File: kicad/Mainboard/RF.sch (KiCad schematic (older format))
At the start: 100 parts, among them J8 Antenna, Q3 BGA6589, T1 AFT05MS004NT1, U5 ADF7021, U6 HMC546MS8GETR, U7 LM2904A, X1 12.288MHz

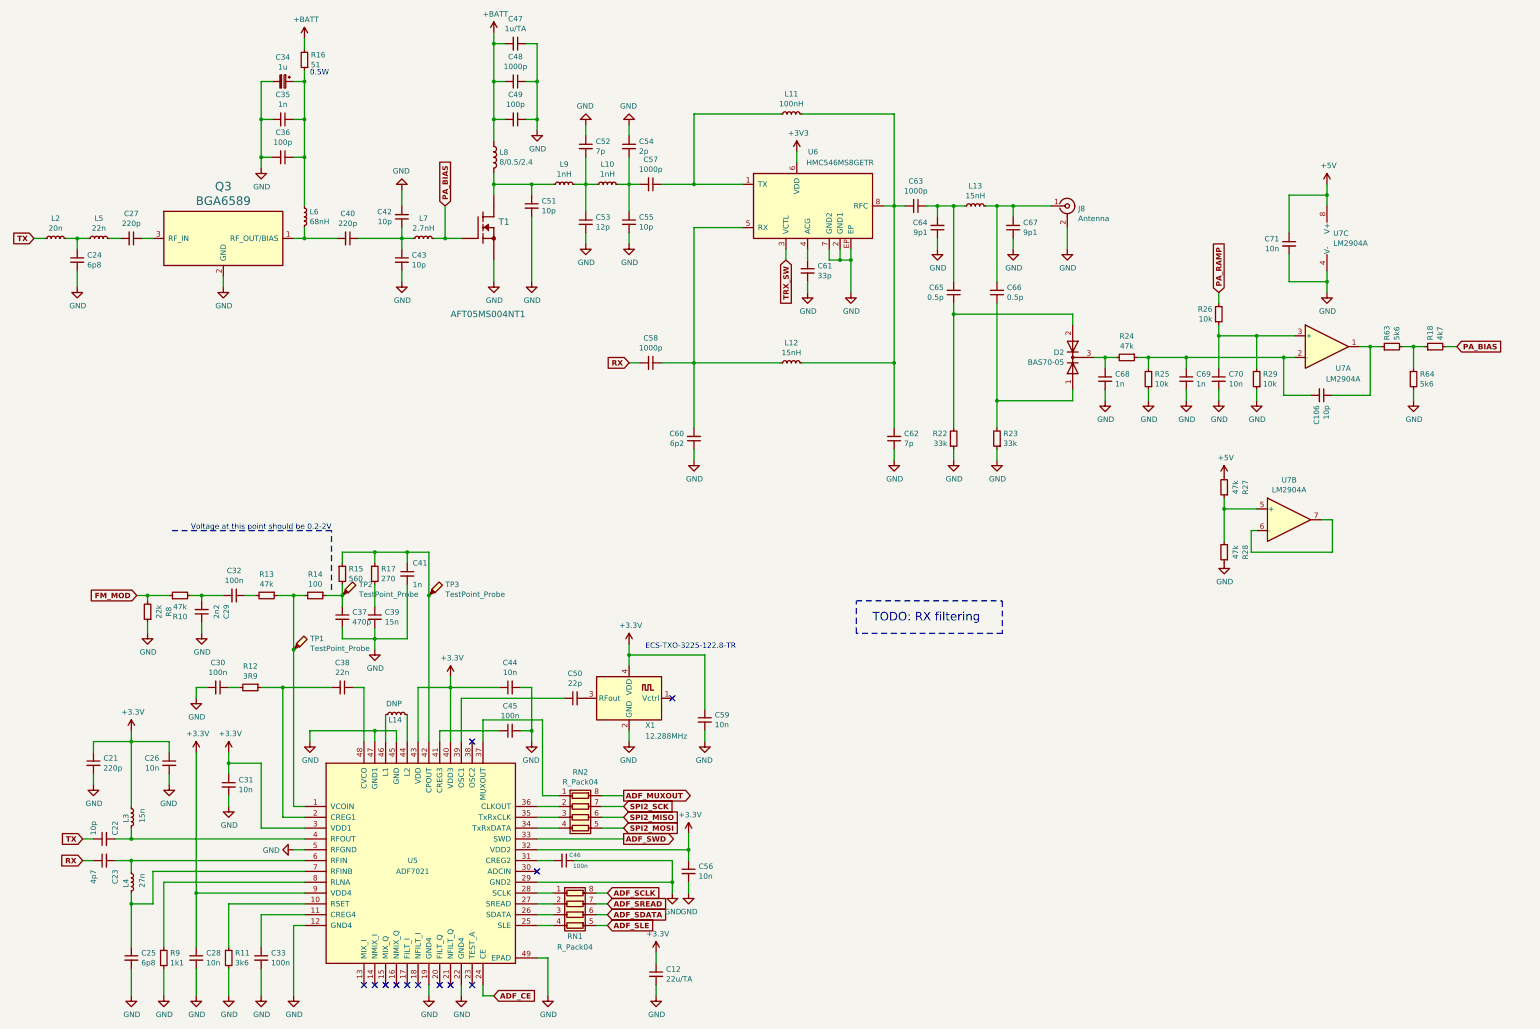
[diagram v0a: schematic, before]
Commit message: added 6 testpoints
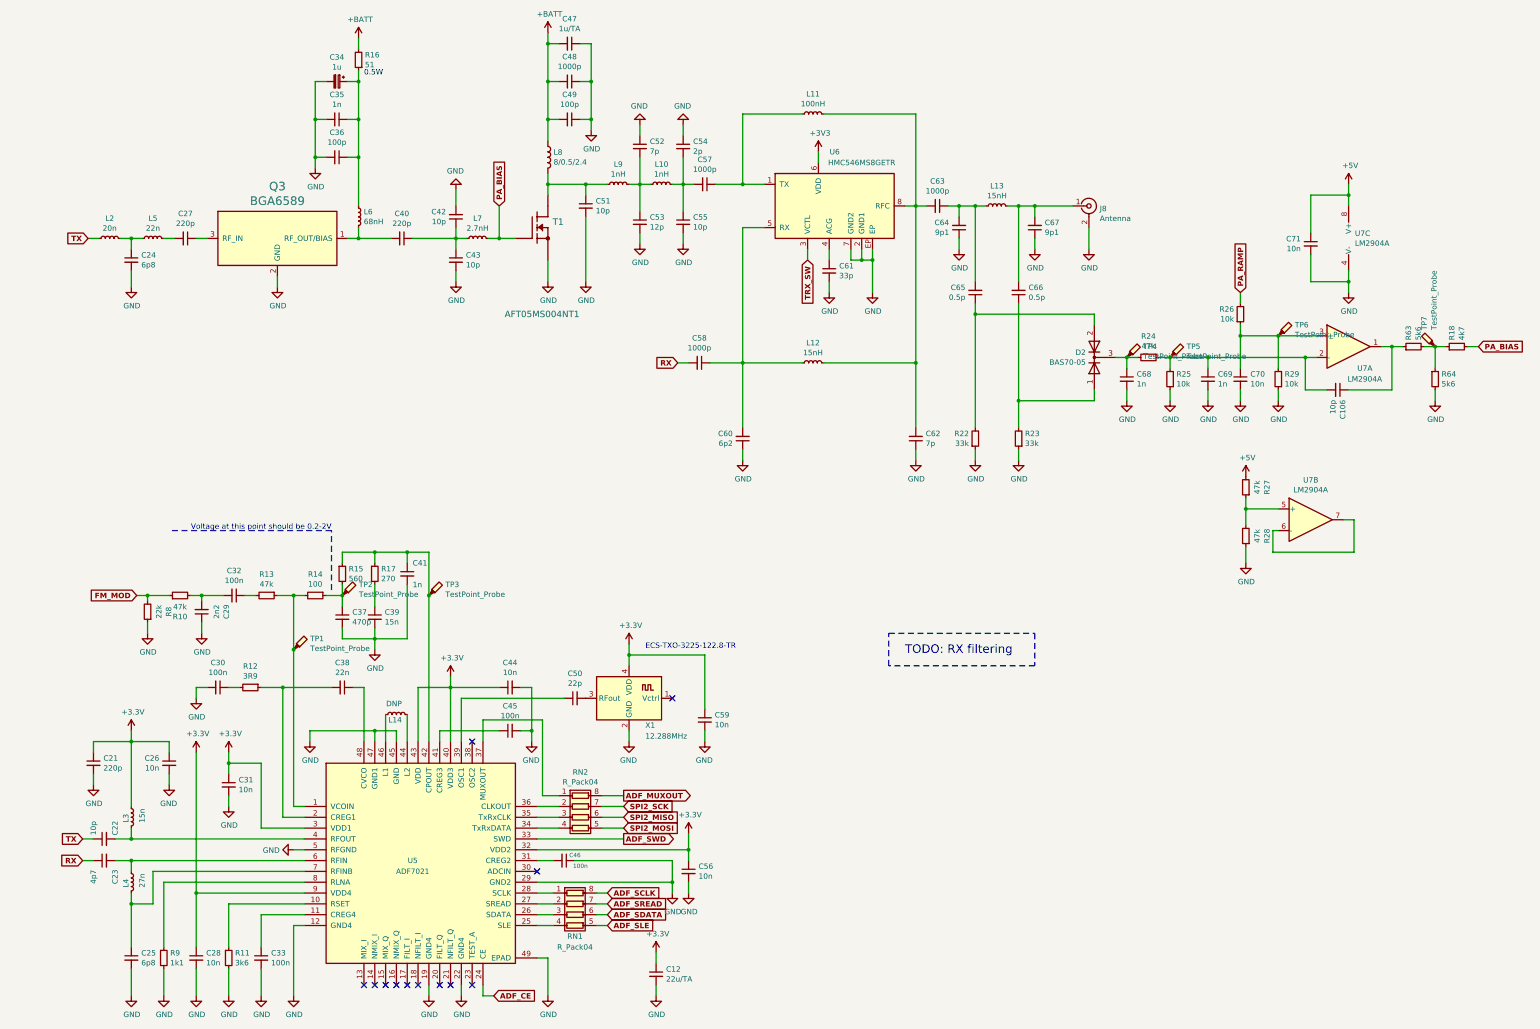
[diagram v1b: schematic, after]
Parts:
- removed C106: 10p, Capacitor_SMD:C_0603_1608Metric, symbol Mainboard-rescue:C_Small-device
- added C106: 10p, Capacitor_SMD:C_0603_1608Metric, symbol Mainboard-rescue:C_Small-Device
- added TP4, TP5, TP6, TP7: TestPoint_Probe, TestPoint:TestPoint_Pad_D1.0mm, symbol Mainboard-rescue:TestPoint_Probe-Connector
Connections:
- net at R18.1, R63.2, R64.1: now also TP7.1
- net at C68.1, D2.3 (K), R24.2: now also TP4.1
- net at C69.1, R24.1, R25.2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: now also C106.2, TP5.1
- net at R63.1, U7.1: now also C106.1
- net at C70.1, R26.1, R29.2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: now also TP6.1
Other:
- moved on the sheet: C24, C27, C34, C35, C36, C40, C42, C43, C47, C48, C49, C51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

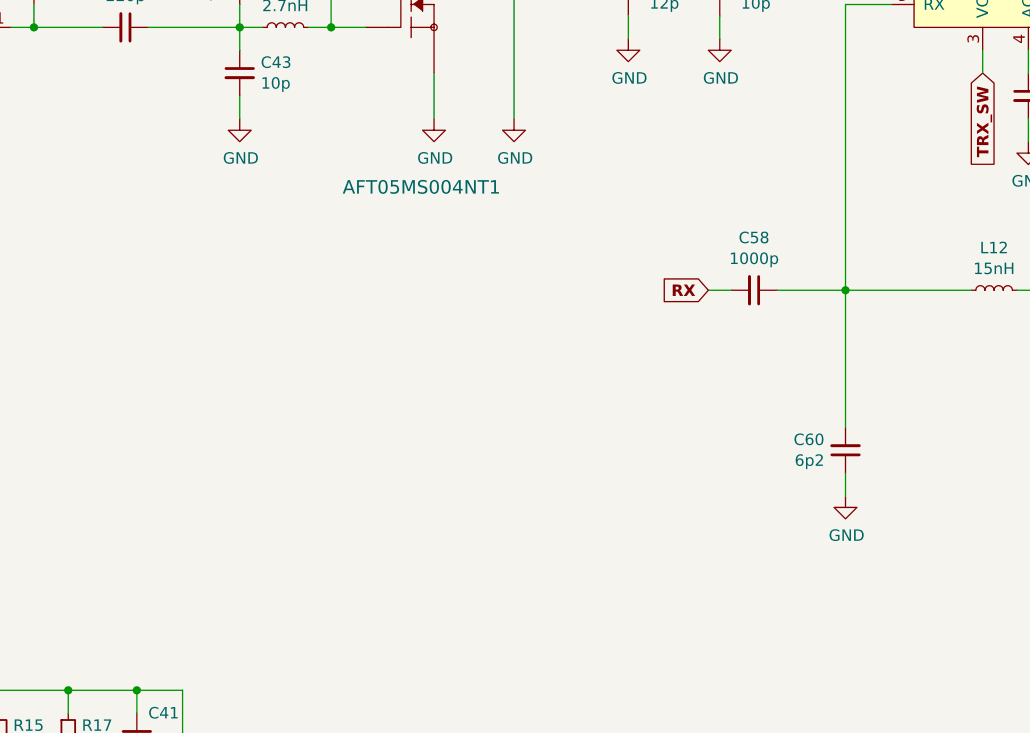
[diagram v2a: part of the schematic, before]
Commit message: added BGA2874 RX amplifier & highpass LC filter(schematic & pcb) pcb design nearly done ~95%
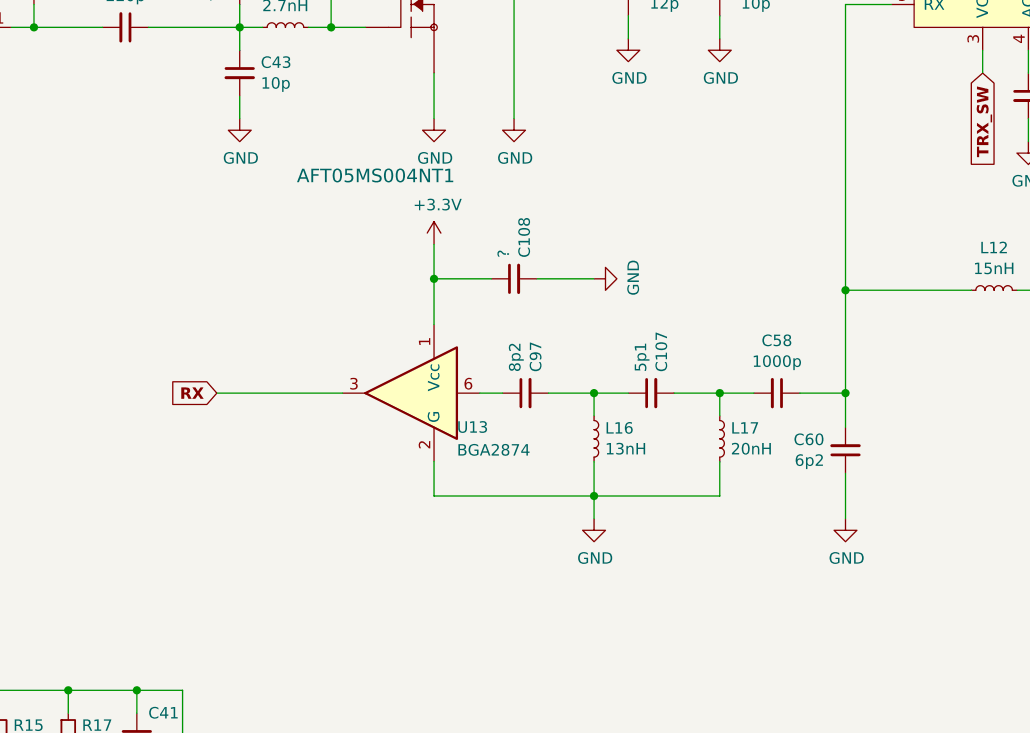
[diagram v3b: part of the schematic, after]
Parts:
- added C107: 5p1, Capacitor_SMD:C_0603_1608Metric, symbol Mainboard-rescue:C_Small-Device
- added C108: ?, Capacitor_SMD:C_0603_1608Metric, symbol Mainboard-rescue:C_Small-Device
- added C97: 8p2, Capacitor_SMD:C_0603_1608Metric, symbol Mainboard-rescue:C_Small-Device
- added L16: 13nH, Inductor_SMD:L_0603_1608Metric, symbol Device:L_Small
- added L17: 20nH, Inductor_SMD:L_0603_1608Metric, symbol Device:L_Small
- added U13: BGA2874, Package_TO_SOT_SMD:SOT-363_SC-70-6, symbol RF_Amplifier:BGA2874
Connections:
- net +3V3: now also C108.1, U13.1 (Vcc)
- net GND: now also C108.2, L16.2, L17.2, U13.2 (G), U13.4 (G), U13.5 (G)
- net RX: now also U13.3; no longer C58.2
- new net: C107.2, C58.2, L17.1
- new net: C97.1, U13.6
- new net: C107.1, C97.2, L16.1
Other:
- moved on the sheet: C58
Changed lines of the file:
@@
 EESchema Schematic File Version 4
-LIBS:Mainboard-cache
 EELAYER 30 0
 EELAYER END
@@
 P 6250 2900
 F 0 "T1" H 6394 2953 59  0000 L CNN
-F 1 "AFT05MS004NT1" H 5950 2100 59  0000 L CNN
+F 1 "AFT05MS004NT1" H 5750 2150 59  0000 L CNN
 F 2 "TR-9:AFT05MS004NT1" H 6250 2900 50  0001 C CNN
 F 3 "" H 6250 2900 50  0001 C CNN
@@
 L Mainboard-rescue:C_Small-device C58
 U 1 1 5DF79664
-P 7750 4150
-F 0 "C58" V 7521 4150 50  0000 C CNN
-F 1 "1000p" V 7612 4150 50  0000 C CNN
-F 2 "Capacitor_SMD:C_0603_1608Metric" H 7750 4150 50  0001 C CNN
-F 3 "~" H 7750 4150 50  0001 C CNN
-	1    7750 4150
+P 7850 4600
+F 0 "C58" V 7621 4600 50  0000 C CNN
+F 1 "1000p" V 7712 4600 50  0000 C CNN
+F 2 "Capacitor_SMD:C_0603_1608Metric" H 7850 4600 50  0001 C CNN
+F 3 "~" H 7850 4600 50  0001 C CNN
+	1    7850 4600
 	0    1    1    0
 $EndComp
@@
 Wire Wire Line
 	8150 2900 8150 4150
-Wire Wire Line
-	7650 4150 7550 4150
-Text GLabel 7550 4150 0    50   Input ~ 10
+Text GLabel 5400 4600 0    50   Input ~ 10
 RX
 Text GLabel 14950 4000 2    50   Input ~ 10
@@
 L power:GND #PWR098
 U 1 1 5E0A2231
-P 8150 5050
-F 0 "#PWR098" H 8150 4800 50  0001 C CNN
-F 1 "GND" H 8155 4877 50  0000 C CNN
-F 2 "" H 8150 5050 50  0001 C CNN
-F 3 "" H 8150 5050 50  0001 C CNN
-	1    8150 5050
-	1    0    0    -1
-$EndComp
-Wire Wire Line
-	8150 4950 8150 5050
-Wire Wire Line
-	8150 4150 8150 4750
+P 8150 5150
+F 0 "#PWR098" H 8150 4900 50  0001 C CNN
+F 1 "GND" H 8155 4977 50  0000 C CNN
+F 2 "" H 8150 5150 50  0001 C CNN
+F 3 "" H 8150 5150 50  0001 C CNN
+	1    8150 5150
+	1    0    0    -1
+$EndComp
+Wire Wire Line
+	8150 4150 8150 4600
 $Comp
 L Mainboard-rescue:C_Small-Device C62
@@
 	8150 2500 8350 2500
 Wire Wire Line
-	7850 4150 8150 4150
-Wire Wire Line
 	8150 4150 8700 4150
 Wire Wire Line
@@
 	0    -1   -1   0
 $EndComp
+$Comp
+L RF_Amplifier:BGA2874 U13
+U 1 1 5EB02D36
+P 6250 4600
+F 0 "U13" H 6050 4450 50  0000 R CNN
+F 1 "BGA2874" H 6050 4350 50  0000 R CNN
+F 2 "Package_TO_SOT_SMD:SOT-363_SC-70-6" H 6200 3950 50  0001 C CNN
+F 3 "https://www.nxp.com/docs/en/data-sheet/BGA2874.pdf" H 6250 4600 50  0001 C CNN
+	1    6250 4600
+	-1   0    0    -1
+$EndComp
+$Comp
+L Device:L_Small L17
+U 1 1 5EB6932C
+P 7600 4800
+F 0 "L17" H 7648 4846 50  0000 L CNN
+F 1 "20nH" H 7648 4755 50  0000 L CNN
+F 2 "Inductor_SMD:L_0603_1608Metric" H 7600 4800 50  0001 C CNN
+F 3 "~" H 7600 4800 50  0001 C CNN
+	1    7600 4800
+	1    0    0    -1
+$EndComp
+$Comp
+L Mainboard-rescue:C_Small-Device C107
+U 1 1 5EB6AF5F
+P 7300 4600
+F 0 "C107" H 7208 4554 50  0000 R CNN
+F 1 "5p1" H 7208 4645 50  0000 R CNN
+F 2 "Capacitor_SMD:C_0603_1608Metric" H 7300 4600 50  0001 C CNN
+F 3 "~" H 7300 4600 50  0001 C CNN
+	1    7300 4600
+	0    -1   1    0
+$EndComp
+$Comp
+L Device:L_Small L16
+U 1 1 5EB6CEAB
+P 7050 4800
+F 0 "L16" H 7098 4846 50  0000 L CNN
+F 1 "13nH" H 7098 4755 50  0000 L CNN
+F 2 "Inductor_SMD:L_0603_1608Metric" H 7050 4800 50  0001 C CNN
+F 3 "~" H 7050 4800 50  0001 C CNN
+	1    7050 4800
+	1    0    0    -1
+$EndComp
+$Comp
+L Mainboard-rescue:C_Small-Device C97
+U 1 1 5EB6D251
+P 6750 4600
+F 0 "C97" H 6658 4554 50  0000 R CNN
+F 1 "8p2" H 6658 4645 50  0000 R CNN
+F 2 "Capacitor_SMD:C_0603_1608Metric" H 6750 4600 50  0001 C CNN
+F 3 "~" H 6750 4600 50  0001 C CNN
+	1    6750 4600
+	0    -1   1    0
+$EndComp
+Wire Wire Line
+	6550 4600 6650 4600
+$Comp
+L power:GND #PWR0120
+U 1 1 5EC16C67
+P 7050 5150
+F 0 "#PWR0120" H 7050 4900 50  0001 C CNN
+F 1 "GND" H 7055 4977 50  0000 C CNN
+F 2 "" H 7050 5150 50  0001 C CNN
+F 3 "" H 7050 5150 50  0001 C CNN
+	1    7050 5150
+	1    0    0    -1
+$EndComp
+Wire Wire Line
+	7950 4600 8150 4600
+Connection ~ 8150 4600
+Wire Wire Line
+	8150 4600 8150 4750
+$Comp
+L power:+3.3V #PWR0176
+U 1 1 5ECF6899
+P 6350 3950
+F 0 "#PWR0176" H 6350 3800 50  0001 C CNN
+F 1 "+3.3V" H 6365 4123 50  0000 C CNN
+F 2 "" H 6350 3950 50  0001 C CNN
+F 3 "" H 6350 3950 50  0001 C CNN
+	1    6350 3950
+	1    0    0    -1
+$EndComp
+$Comp
+L Mainboard-rescue:C_Small-Device C108
+U 1 1 5ED2084B
+P 6700 4100
+F 0 "C108" H 6608 4054 50  0000 R CNN
+F 1 "?" H 6608 4145 50  0000 R CNN
+F 2 "Capacitor_SMD:C_0603_1608Metric" H 6700 4100 50  0001 C CNN
+F 3 "~" H 6700 4100 50  0001 C CNN
+	1    6700 4100
+	0    -1   1    0
+$EndComp
+Connection ~ 6350 4100
+$Comp
+L power:GND #PWR0177
+U 1 1 5ED3FE5B
+P 7050 4100
+F 0 "#PWR0177" H 7050 3850 50  0001 C CNN
+F 1 "GND" H 7055 3927 50  0000 C CNN
+F 2 "" H 7050 4100 50  0001 C CNN
+F 3 "" H 7050 4100 50  0001 C CNN
+	1    7050 4100
+	0    -1   -1   0
+$EndComp
+Wire Wire Line
+	5400 4600 5950 4600
+Wire Wire Line
+	6800 4100 7050 4100
+Wire Wire Line
+	6350 4100 6600 4100
+Wire Wire Line
+	6350 3950 6350 4100
+Wire Wire Line
+	6350 4100 6350 4300
+Wire Wire Line
+	6850 4600 7050 4600
+Wire Wire Line
+	7050 4700 7050 4600
+Connection ~ 7050 4600
+Wire Wire Line
+	7050 4600 7200 4600
+Wire Wire Line
+	7400 4600 7600 4600
+Wire Wire Line
+	7600 4700 7600 4600
+Connection ~ 7600 4600
+Wire Wire Line
+	7600 4600 7750 4600
+Wire Wire Line
+	8150 4950 8150 5150
+Wire Wire Line
+	7600 4900 7600 5050
+Wire Wire Line
+	7600 5050 7050 5050
+Wire Wire Line
+	6350 5050 6350 4900
+Wire Wire Line
+	7050 4900 7050 5050
+Connection ~ 7050 5050
+Wire Wire Line
+	7050 5050 6350 5050
+Wire Wire Line
+	7050 5050 7050 5150
 $EndSCHEMATC
